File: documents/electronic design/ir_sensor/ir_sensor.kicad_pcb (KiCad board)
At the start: 2 copper layers, 8 parts, among them U1 TL1838, U2 STM32F103HEADER, U3 MPU6050_module, U4 SE8R01_module

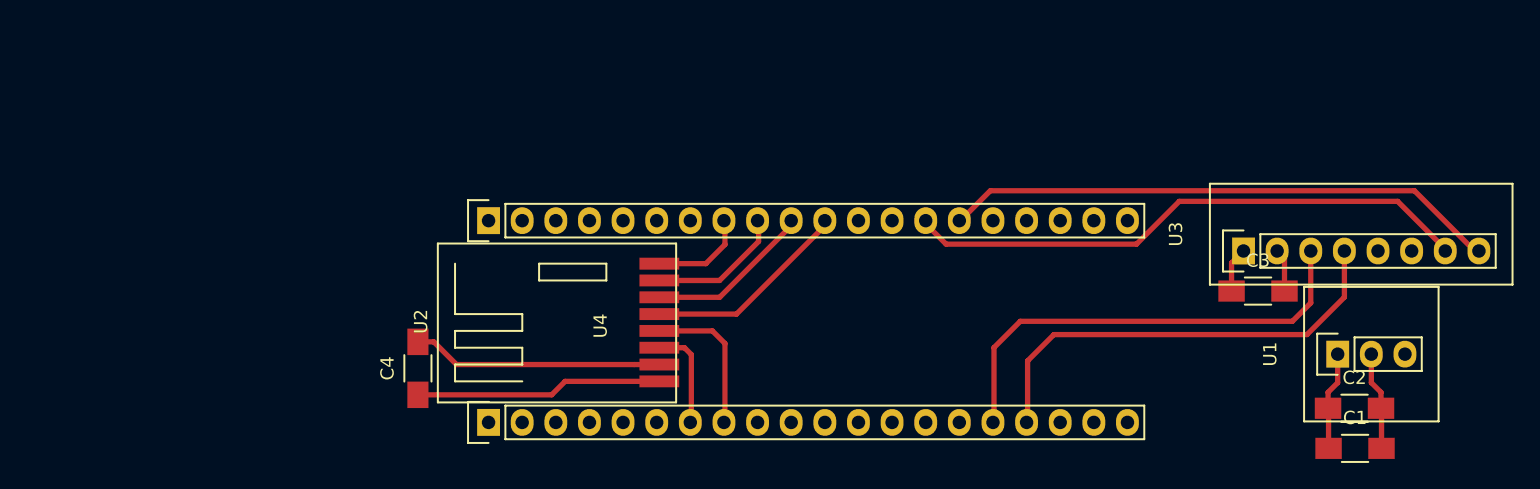
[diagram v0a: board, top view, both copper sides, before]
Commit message: make double-sided PCB for beamer; make pcb for receiver
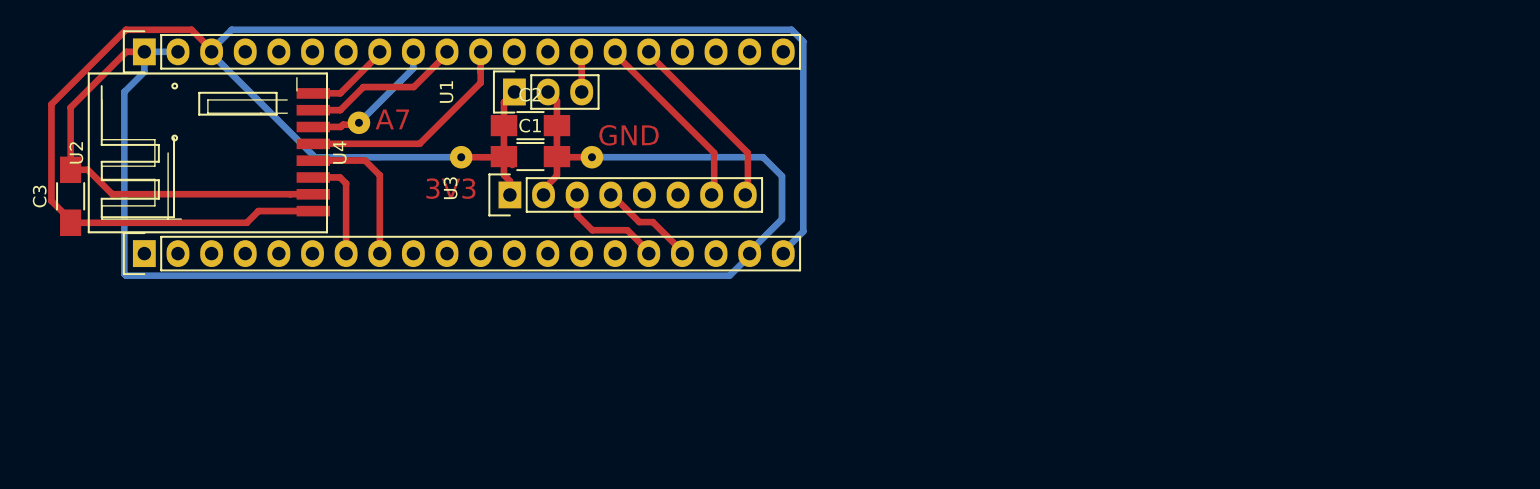
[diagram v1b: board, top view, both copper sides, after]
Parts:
- removed C4: 100uf, Capacitors_SMD:C_1206_HandSoldering
- added P1: Via, footprints:Via, F.Cu at (98.4, 54.6)
- added P2: Via, footprints:Via, F.Cu at (116.0, 57.2)
- added P3: Via, footprints:Via, F.Cu at (106.1, 57.2)
- U4: footprint footprints:SE8R01 -> footprints:SE8R01_SMD
- moved C3 90.0 mm to (76.6, 60.1), turned to 90 degrees
- moved C1 66.1 mm to (111.4, 57.1)
- moved C2 65.8 mm to (111.4, 54.8)
- moved U1 65.3 mm to (110.1, 52.3)
- moved U3 55.6 mm to (109.8, 60.0)
- moved U4 30.2 mm to (96.0, 62.9)
- moved U2 29.0 mm to (82.2, 64.5)
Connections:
- U2 pad 29: SPI_MISO -> SPI_MOSI
- U2 pad 30: SPI_MOSI -> SPI_MISO
- U2 pad 34: AD0 -> IR_RCV
- U2 pad 35: MPU5060_INT -> AD0
- U2 pad 36: Net-(U2-Pad36) -> MPU5060_INT
- U2 pad 5: IR_RCV -> Net-(U2-Pad5)
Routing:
- net +3V3: track 29.5 -> 140.7 mm
- net GND: track 29.6 -> 132.1 mm
- net AD0: track 42.9 -> 13.9 mm
- net MPU5060_INT: track 42.1 -> 13.9 mm
- net I2C_SDA: track 34.2 -> 7.33 mm
- net I2C_SCL: track 35.1 -> 8.22 mm
- net IR_RCV: track 0.00 -> 3.10 mm
- net SPI_MISO: track 10.1 -> 12.0 mm
- net SPI_MOSI: track 12.5 -> 10.6 mm
- net SPI_SCK: track 15.5 -> 16.9 mm
- net SE8R01_IRQ: track 7.20 -> 6.38 mm
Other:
- net class Default: trace_width 0.4 -> 0.5
- board text added: "3V3"
- board text added: "A7"
- board text added: "GND"

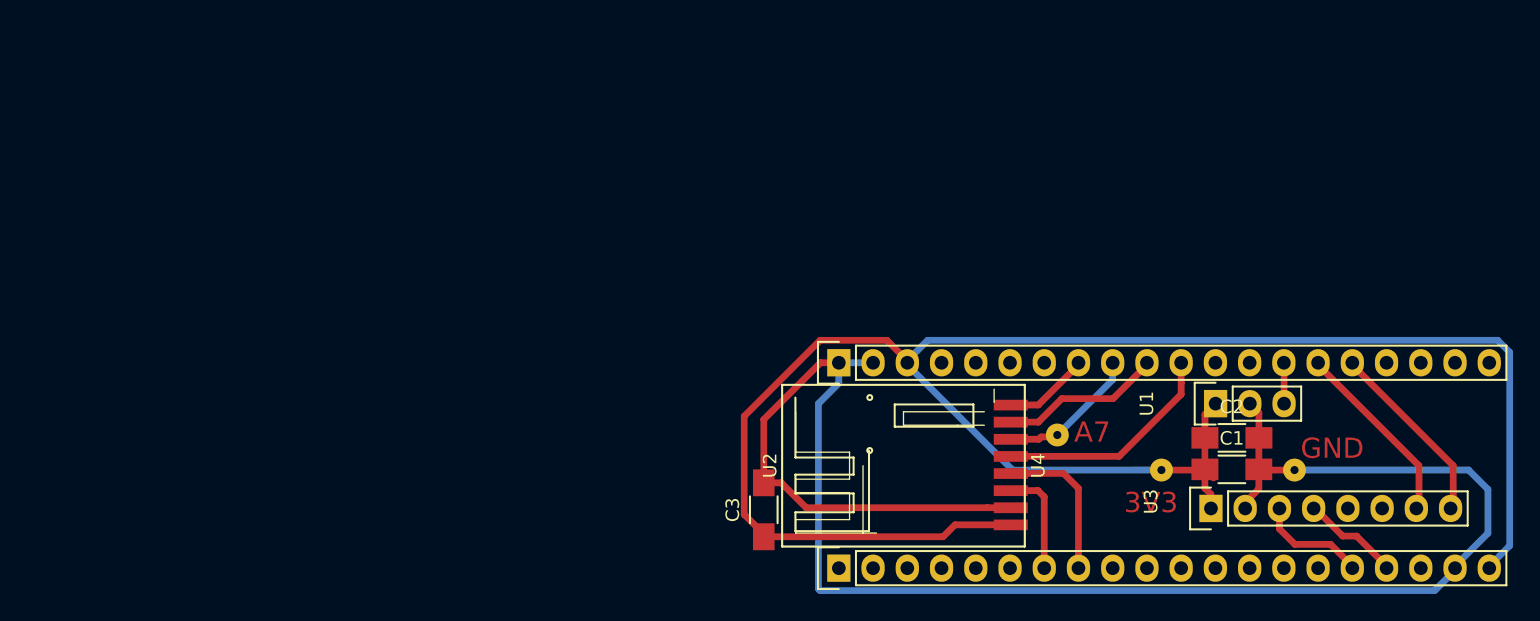
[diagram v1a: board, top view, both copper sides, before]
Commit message: update PCB projects for beamer and sensor
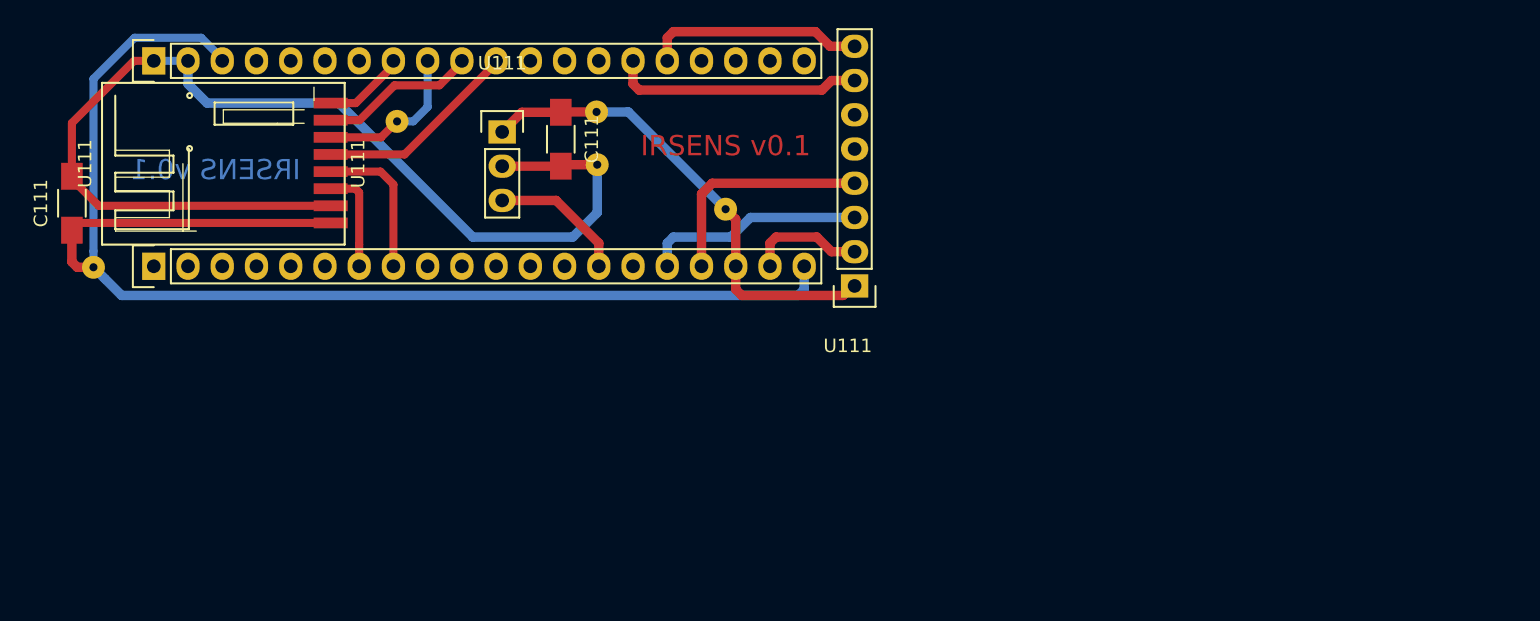
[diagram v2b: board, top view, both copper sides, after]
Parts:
- removed C1: 104, Capacitors_SMD:C_1206_HandSoldering
- removed C2, C3: 100uf, Capacitors_SMD:C_1206_HandSoldering
- removed P1, P2, P3: Via, footprints:Via
- removed U1: TL1838, footprints:TL1838_footprint
- removed U2: STM32F103HEADER, footprints:STM32F103_header_footprint
- removed U3: MPU6050_module, footprints:MPU6050_pin_header_straight
- removed U4: SE8R01_module, footprints:SE8R01_SMD
- added C111: 100uf, Capacitors_SMD:C_1206_HandSoldering, F.Cu at (61.6, 32.7)
- added C111: 100uf, Capacitors_SMD:C_1206_HandSoldering, F.Cu at (25.3, 37.4)
- added P111: Via, footprints:Via, F.Cu at (49.4, 31.3)
- added P111: Via, footprints:Via, F.Cu at (64.3, 34.5)
- added P111: Via, footprints:Via, F.Cu at (64.2, 30.6)
- added P111: Via, footprints:Via, F.Cu at (26.9, 42.2)
- added P111: Via, footprints:Via, F.Cu at (73.8, 37.8)
- added U111: STM32F103HEADER, footprints:STM32F103_header_footprint, F.Cu at (31.4, 42.1)
- added U111: TL1838, footprints:TL1838_footprint, F.Cu at (57.2, 32.1)
- added U111: MPU6050_module, footprints:MPU6050_pin_header_straight, F.Cu at (83.4, 43.5)
- added U111: SE8R01_module, footprints:SE8R01_SMD, F.Cu at (45.5, 40.5)
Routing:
- net GND: track 132.1 -> 91.5 mm
- net +3V3: track 140.7 -> 103.9 mm
- net +5V: track 0.00 -> 35.7 mm
- net I2C_SDA: track 7.33 -> 17.1 mm
- net I2C_SCL: track 8.22 -> 16.4 mm
- net IR_RCV: track 3.10 -> 10.2 mm
- net AD0: track 13.9 -> 18.6 mm
- net MPU5060_INT: track 13.9 -> 16.3 mm
- net SPI_SCK: track 16.9 -> 15.2 mm
- net SPI_MOSI: track 10.6 -> 11.6 mm
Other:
- board text added: "IRSENS v0.1"
- board text removed: "3V3"
- board text removed: "A7"
- board text removed: "GND"

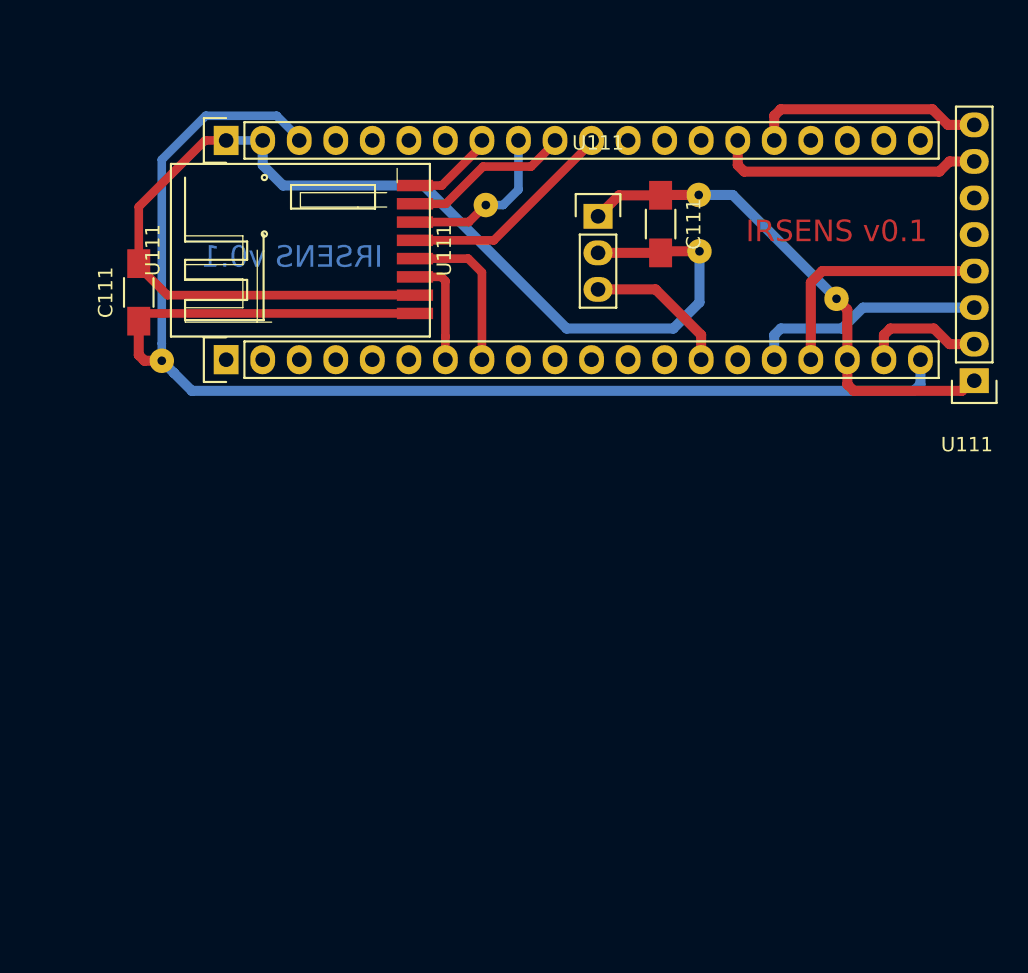
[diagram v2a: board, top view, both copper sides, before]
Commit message: update pin mapping, regenerate for i2c2,spi2, number of tim input channels. WIP
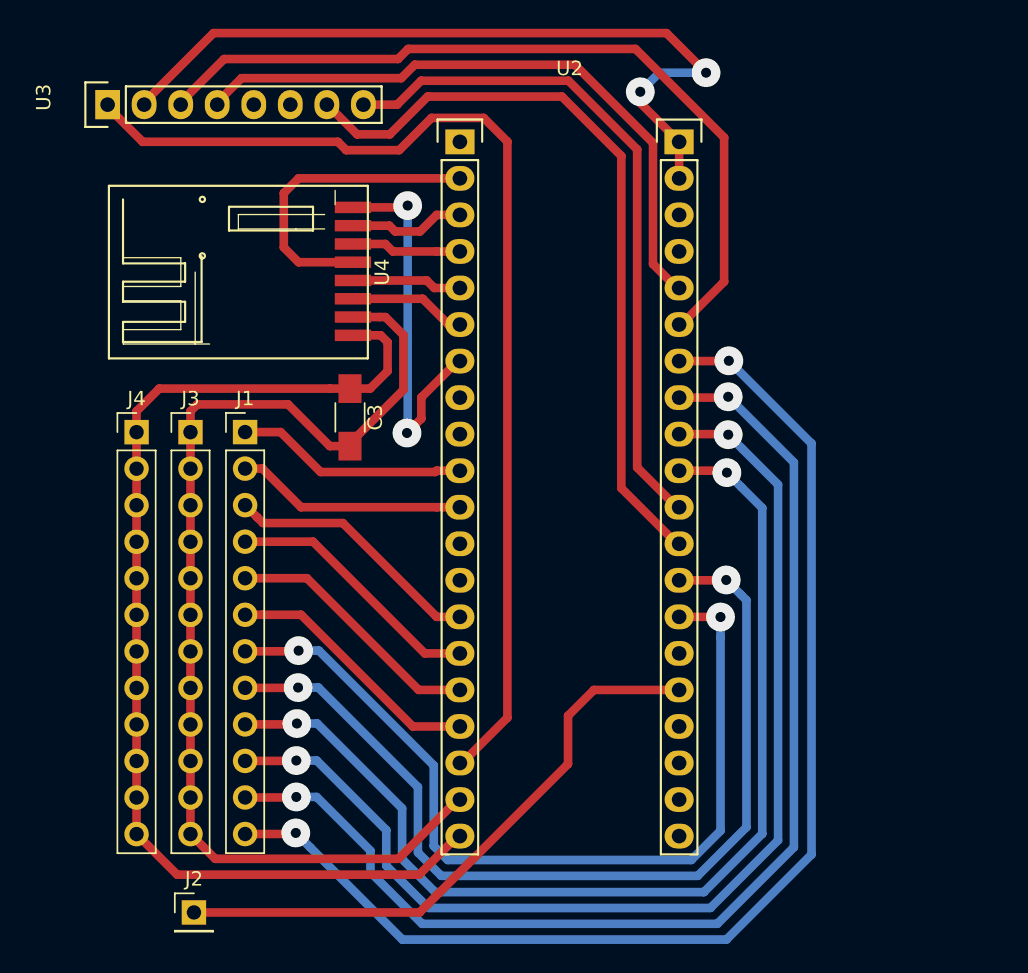
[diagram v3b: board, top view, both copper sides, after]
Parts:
- removed C111 (x2): 100uf, Capacitors_SMD:C_1206_HandSoldering
- removed P111 (x5): Via, footprints:Via
- removed U111: STM32F103HEADER, footprints:STM32F103_header_footprint
- removed U111: TL1838, footprints:TL1838_footprint
- removed U111: MPU6050_module, footprints:MPU6050_pin_header_straight
- removed U111: SE8R01_module, footprints:SE8R01_SMD
- added C3: 100uf, Capacitors_SMD:C_1206_HandSoldering, F.Cu at (40.0, 46.1)
- added J1: Conn_01x12, Pin_Headers:Pin_Header_Straight_1x12_Pitch2.54mm, F.Cu at (32.7, 47.1)
- added J2: Conn_01x01, Pin_Headers:Pin_Header_Straight_1x01_Pitch2.54mm, F.Cu at (29.1, 80.5)
- added J3: Conn_01x12, Pin_Headers:Pin_Header_Straight_1x12_Pitch2.54mm, F.Cu at (28.9, 47.1)
- added J4: Conn_01x12, Pin_Headers:Pin_Header_Straight_1x12_Pitch2.54mm, F.Cu at (25.1, 47.1)
- added U2: STM32F103HEADER, footprints:STM32F103_header_footprint, F.Cu at (47.6, 26.9)
- added U3: MPU6050_module, footprints:MPU6050_pin_header_straight, F.Cu at (23.1, 24.4)
- added U4: SE8R01_module, footprints:SE8R01_SMD, F.Cu at (41.2, 42.0)
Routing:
- net input_6: track 0.00 -> 85.1 mm, vias 0 -> 2
- net input_5: track 0.00 -> 81.5 mm, vias 0 -> 2
- net input_4: track 0.00 -> 77.8 mm, vias 0 -> 2
- net input_3: track 0.00 -> 74.1 mm, vias 0 -> 2
- net input_2: track 0.00 -> 65.4 mm, vias 0 -> 2
- net input_1: track 0.00 -> 61.0 mm, vias 0 -> 2
- net LED_DBG: track 0.00 -> 42.1 mm
- net I2C_SCL: track 16.4 -> 56.4 mm
- net +5V: track 35.7 -> 75.5 mm
- net GND: track 91.5 -> 130.9 mm, vias 0 -> 2
- net AD0: track 18.6 -> 52.8 mm
- net MPU5060_INT: track 16.3 -> 47.9 mm
- net I2C_SDA: track 17.1 -> 44.7 mm
- net +3V3: track 103.9 -> 77.4 mm
- net SE8R01_IRQ: track 6.15 -> 26.3 mm, vias 0 -> 2
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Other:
- net class Default: clearance 0.4 -> 0.3; trace_width 0.5 -> 0.6; via_dia 0.6 -> 2; via_drill 0.4 -> 0.7
- net class Thick added: clearance 0.5, trace_width 0.7, via_dia 1.5, via_drill 0.6
- net class Thin added: clearance 0.2, trace_width 0.3, via_dia 1.5, via_drill 0.6
- rule trace_clearance: 0.4 -> 0.3
- board text removed: "IRSENS v0.1"

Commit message: adjust pcb design
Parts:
- added J5: Conn_01x06, Pin_Headers:Pin_Header_Straight_1x06_Pitch2.54mm, F.Cu at (72.3, 43.9)
- added J6: Conn_01x06, Pin_Headers:Pin_Header_Straight_1x06_Pitch2.54mm, F.Cu at (25.2, 47.1)
- added J7: Conn_01x06, Pin_Headers:Pin_Header_Straight_1x06_Pitch2.54mm, F.Cu at (76.0, 43.9)
- J1, J3, J4: value Conn_01x12 -> Conn_01x06; footprint Pin_Headers:Pin_Header_Straight_1x12_Pitch2.54mm -> Pin_Headers:Pin_Header_Straight_1x06_Pitch2.54mm
- moved J2 42.3 mm to (68.5, 65.1)
- moved J1 37.1 mm to (68.5, 56.6), turned to 180 degrees
- moved J3 3.79 mm to (32.7, 47.1)
- moved J4 3.78 mm to (28.9, 47.1)
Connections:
- J1 pad 1: input_12 -> input_1
- J1 pad 2: input_11 -> input_2
- J1 pad 3: input_7 -> input_3
- J1 pad 4: input_8 -> input_4
- J1 pad 5: input_9 -> input_5
- J1 pad 6: input_10 -> input_6
- J3 pad 1: GND -> input_12
- J3 pad 2: GND -> input_11
- J3 pad 3: GND -> input_7
- J3 pad 4: GND -> input_8
- J3 pad 5: GND -> input_9
- J3 pad 6: GND -> input_10
- J4 pad 1: +3V3 -> GND
- J4 pad 2: +3V3 -> GND
- J4 pad 3: +3V3 -> GND
- J4 pad 4: +3V3 -> GND
- J4 pad 5: +3V3 -> GND
- J4 pad 6: +3V3 -> GND
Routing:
- net +3V3: track 77.4 -> 183.8 mm, vias 0 -> 2
- net GND: track 130.9 -> 225.9 mm, vias 2 -> 4
- net input_6: track 85.1 -> 6.42 mm, vias 2 -> 0
- net input_5: track 81.5 -> 6.42 mm, vias 2 -> 0
- net input_4: track 77.8 -> 6.42 mm, vias 2 -> 0
- net input_3: track 74.1 -> 6.42 mm, vias 2 -> 0
- net input_2: track 65.4 -> 7.07 mm, vias 2 -> 0
- net input_1: track 61.0 -> 7.07 mm, vias 2 -> 0
- net LED_DBG: track 42.1 -> 5.66 mm
- net I2C_SCL: track 56.4 -> 59.1 mm

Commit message: adjust pcb design
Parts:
- moved J6 7.35 mm to (30.9, 51.8)
- moved J4 7.33 mm to (34.6, 51.8)
- moved J3 7.31 mm to (38.3, 51.8)
- moved U4 1.70 mm to (39.6, 42.4)
- moved C3 0.91 mm to (39.2, 45.6), turned to 0 degrees
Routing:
- net GND: track 225.9 -> 192.8 mm
- net +3V3: track 183.8 -> 153.2 mm
- net SE8R01_IRQ: track 26.3 -> 18.2 mm
- net input_10: track 18.1 -> 10.6 mm
- net input_9: track 18.1 -> 10.6 mm
- net input_8: track 18.1 -> 10.6 mm
- net input_7: track 18.2 -> 10.8 mm
- net SPI_SCK: track 21.7 -> 15.4 mm, vias 0 -> 2
- net input_12: track 16.3 -> 10.3 mm
- net input_11: track 16.0 -> 10.3 mm
- net I2C_SDA: track 44.7 -> 47.2 mm
- net SE8R01_CE: track 8.18 -> 10.5 mm
- net AD0: track 52.8 -> 50.8 mm
- net SPI_MOSI: track 7.65 -> 9.66 mm
- net SE8R01_CSN: track 7.65 -> 9.62 mm
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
